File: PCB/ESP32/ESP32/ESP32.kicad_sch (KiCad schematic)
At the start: 31 parts, among them J1 Camera_Receptacle_THT, J1 Conn_01x02_Pin, J1 USB_B_Micro, J2 Conn_01x02_Socket, SW1 RESET, SW2 BOOT, SW3 LRA Switch, U1 DRV2605LTDGSRQ1, U1 ESP32-S2-SOLO-U-N4, U1 MCP73832T-2ACI/OT

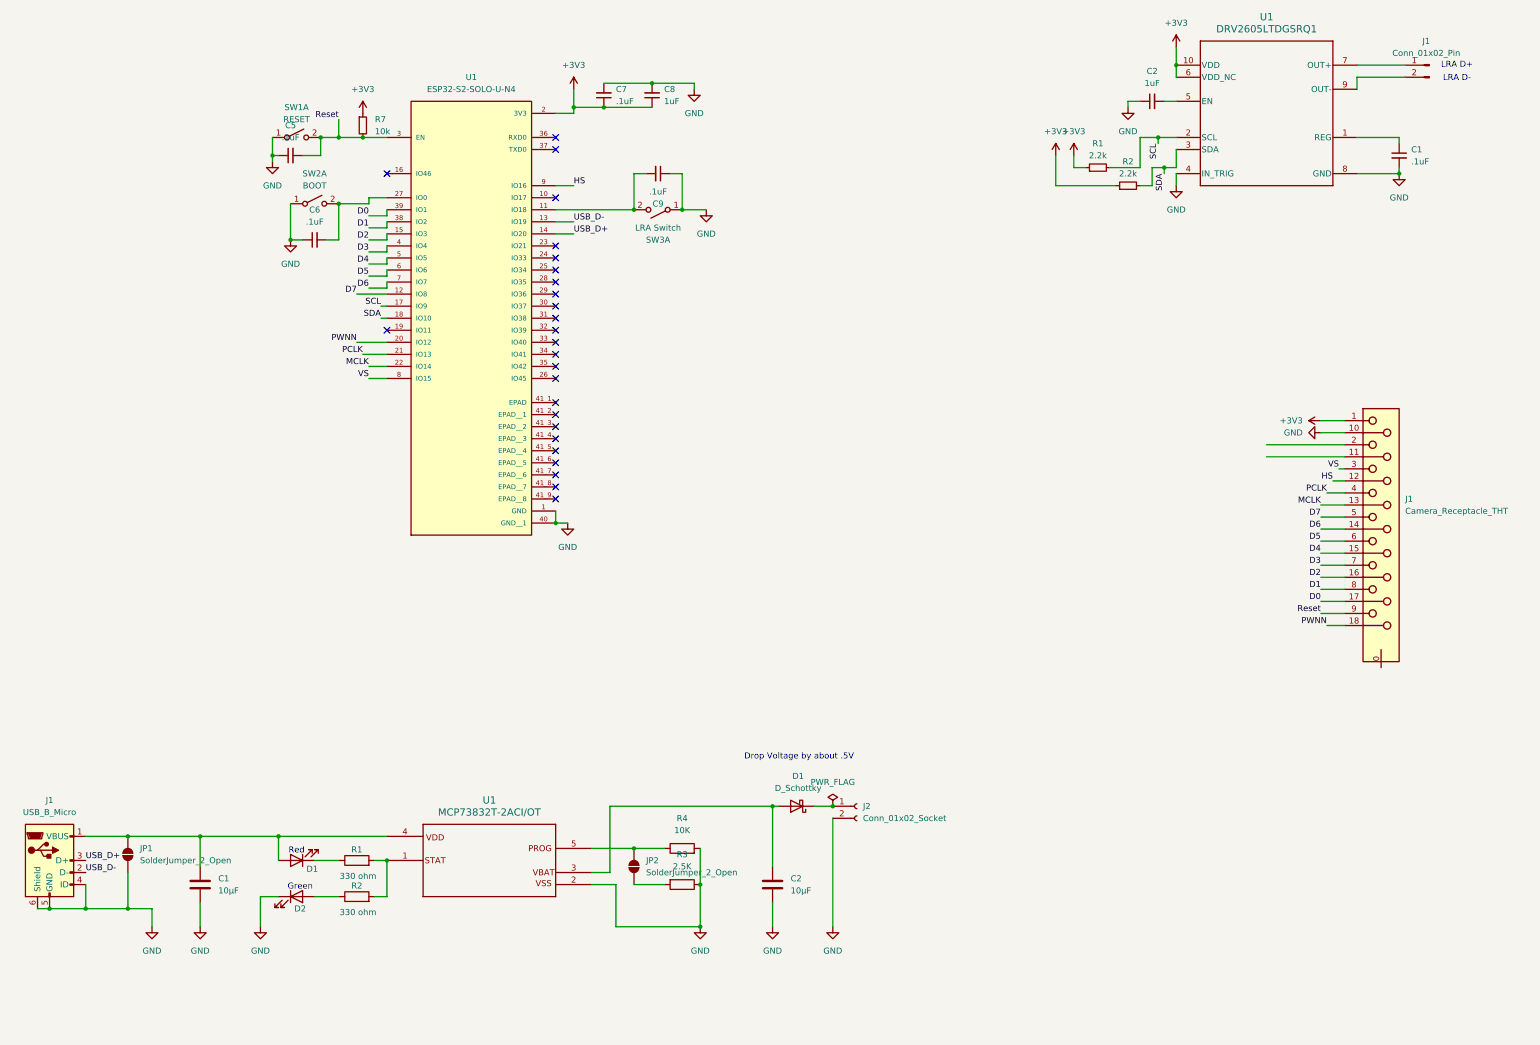
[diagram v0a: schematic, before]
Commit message: Updated camera
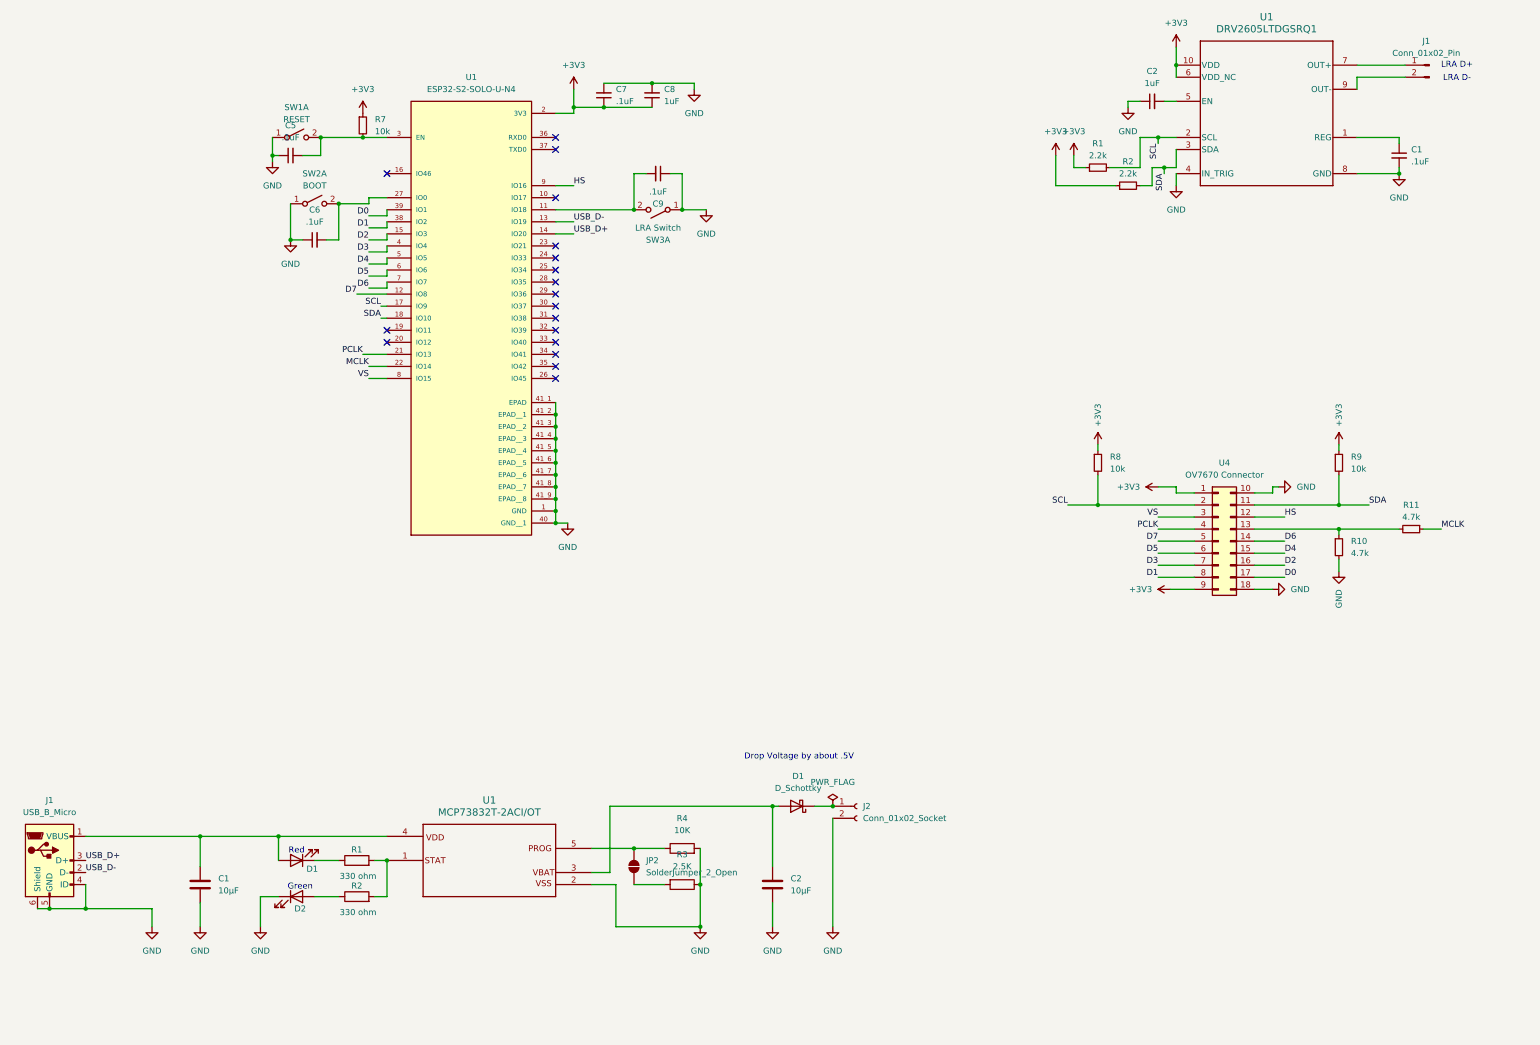
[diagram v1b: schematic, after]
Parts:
- removed J1: Camera_Receptacle_THT, symbol Connector:DA15_Receptacle_MountingHoles
- removed JP1: SolderJumper_2_Open, Jumper:SolderJumper-2_P1.3mm_Bridged2Bar_Pad1.0x1.5mm, symbol Jumper:SolderJumper_2_Open
- added R10, R11: 4.7k, Resistor_SMD:R_0603_1608Metric, symbol Device:R_Small
- added R8, R9: 10k, Resistor_SMD:R_0805_2012Metric, symbol Device:R_Small
- added U4: OV7670 Connector, symbol Connector_Generic:Conn_02x09_Top_Bottom
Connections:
- net +3V3: now also R8.1, R9.1, U4.1 (Pin_1), U4.9 (Pin_9)
- net D0: now also U4.17 (Pin_17)
- net D1: now also U4.8 (Pin_8)
- net D2: now also U4.16 (Pin_16)
- net D3: now also U4.7 (Pin_7)
- net D4: now also U4.15 (Pin_15)
- net D5: now also U4.6 (Pin_6)
- net D6: now also U4.14 (Pin_14)
- net D7: now also U4.5 (Pin_5)
- net GND: now also U1.41_1 (EPAD), U1.41_2 (EPAD__1), U1.41_3 (EPAD__2), U1.41_4 (EPAD__3), U1.41_5 (EPAD__4), U1.41_6 (EPAD__5), U1.41_7 (EPAD__6), U1.41_8 (EPAD__7), U1.41_9 (EPAD__8), R10.2, U4.10 (Pin_10), U4.18 (Pin_18)
- net HS: now also U4.12 (Pin_12)
- net MCLK: now also R11.1
- net PCLK: now also U4.4 (Pin_4)
- net SCL: now also R8.2, U4.2 (Pin_2)
- net SDA: now also R9.2, U4.11 (Pin_11)
- net VS: now also U4.3 (Pin_3)
- net PWNN: no longer names the net of U1.20 (IO12)
- net Reset: no longer names the net of C5.2, R7.2, SW1.2 (B), U1.3 (EN)
- new net: R10.1, R11.2, U4.13 (Pin_13)
- no-connect marks 26 -> 18

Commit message: Charging schematic done
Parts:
- removed C1, C2: 10μF, Capacitor_SMD:C_0603_1608Metric_Pad1.08x0.95mm_HandSolder, symbol Device:C
- removed D1, D2: LED, Diode_SMD:D_0603_1608Metric_Pad1.05x0.95mm_HandSolder, symbol Device:LED
- removed J1: USB_B_Micro, ESP32_sym_footprint:CONN_10118193-0001LF_AMP, symbol Connector:USB_B_Micro
- removed J2: Conn_01x02_Socket, ESP32_sym_footprint:CONN2_B2B-PH-K-S_JST, symbol Connector:Conn_01x02_Socket
- removed R1, R2: 330 ohm, Resistor_SMD:R_0603_1608Metric_Pad0.98x0.95mm_HandSolder, symbol Device:R
- removed R3: 2.5K, Resistor_SMD:R_0603_1608Metric_Pad0.98x0.95mm_HandSolder, symbol Device:R
- added C3, C4: 1uF, symbol Device:C
- added C8: 10μF, Capacitor_SMD:C_0603_1608Metric_Pad1.08x0.95mm_HandSolder, symbol Device:C
- added D4, D5: LED, Diode_SMD:D_0603_1608Metric_Pad1.05x0.95mm_HandSolder, symbol Device:LED
- added J4: Conn_01x02_Socket, ESP32_sym_footprint:CONN2_B2B-PH-K-S_JST, symbol Connector:Conn_01x02_Socket
- added J5: USB_B_Micro, ESP32_sym_footprint:CONN_10118193-0001LF_AMP, symbol Connector:USB_B_Micro
- added Q1: PMOS, symbol Simulation_SPICE:PMOS
- added R12, R13: 330 ohm, Resistor_SMD:R_0603_1608Metric_Pad0.98x0.95mm_HandSolder, symbol Device:R
- added R18: 10K, Resistor_SMD:R_0603_1608Metric_Pad0.98x0.95mm_HandSolder, symbol Device:R
- added R19: 2.5K, Resistor_SMD:R_0603_1608Metric_Pad0.98x0.95mm_HandSolder, symbol Device:R
- added U3: AP2112K-3.3, Package_TO_SOT_SMD:SOT-23-5, symbol Regulator_Linear:AP2112K-3.3
- D1: footprint ESP32_sym_footprint:DO-41_STM -> (none)
- R4: value 10K -> 10k; footprint Resistor_SMD:R_0603_1608Metric_Pad0.98x0.95mm_HandSolder -> (none)
- U1: footprint ESP32_sym_footprint:SOT-23-5_MC_MCH -> SOT-23-5_MC_MCH
- renumbered C5 to C2, C6 to C3, C7 to C4, C8 to C5, C9 to C6, R9 to R14, R10 to R15, R11 to R16, R7 to R3, R8 to R9, U1 to U2, U4 to U3
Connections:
- net GND: now also C3.1, C4.2, C8.2, D5.1 (K), J4.2 (Pin_2), J5.4 (ID), J5.5 (GND), J5.6 (Shield), R18.2, R19.1, U3.2 (GND)
- net USB_D+: now also J5.3 (D+)
- net USB_D-: now also J5.2 (D-)
- net at JP2.1 (A): now also R19.2
- net at JP2.2 (B), U1.5: now also R18.1; no longer R4.1
- net at U1.4: now also D1.2 (A), R4.1, D4.2 (A), J5.1 (VBUS), Q1.2 (G)
- net at D1.1 (K): now also C4.1, U3.5 (VOUT)
- net at U1.3: now also C8.1, J4.1 (Pin_1), Q1.3 (S); no longer D1.2 (A)
- net at U1.1: now also R12.2, R13.2
- new net: C3.2, Q1.1 (D), U3.1 (VIN)
- new net: D4.1 (K), R12.1
- new net: D5.2 (A), R13.1
- new net VCC: U3.3 (EN)
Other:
- note removed: "Drop Voltage by about .5V"

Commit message: ddasd
as
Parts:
- added U1: AP2112K-3.3, Package_TO_SOT_SMD:SOT-23-5, symbol Regulator_Linear:AP2112K-3.3
- C1, C2, C3, C4, C5, C6: footprint Capacitor_SMD:C_0603_1608Metric -> Capacitor_SMD:C_0603_1608Metric_Pad1.08x0.95mm_HandSolder
- C3, C4: footprint (none) -> Capacitor_SMD:C_0603_1608Metric_Pad1.08x0.95mm_HandSolder
- D1: footprint (none) -> zzzzz:SOT-23-5_MC_MCH
- J1, J4: footprint ESP32_sym_footprint:CONN2_B2B-PH-K-S_JST -> zzzzz:CONN2_B2B-PH-K-S_JST
- J5: footprint ESP32_sym_footprint:CONN_10118193-0001LF_AMP -> zzzzz:CONN_10118193-0001LF_AMP
- R1, R14, R2, R3, R9: footprint Resistor_SMD:R_0805_2012Metric -> Resistor_SMD:R_0603_1608Metric_Pad0.98x0.95mm_HandSolder
- R15, R16: footprint Resistor_SMD:R_0603_1608Metric -> Resistor_SMD:R_0603_1608Metric_Pad0.98x0.95mm_HandSolder
- R4: footprint (none) -> Resistor_SMD:R_0603_1608Metric_Pad0.98x0.95mm_HandSolder
- U1: footprint SOT-23-5_MC_MCH -> zzzzz:SOT-23-5_MC_MCH
- U1: footprint ESP32_sym_footprint:DGS0010A_L -> zzzzz:DGS0010A_L
- U3: footprint (none) -> zzzzz:215307-9_TYC
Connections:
- net +3V3: now also C4.1, D1.1 (K), U3.5 (VOUT)
- net GND: now also U1.2 (GND)
- net at D4.2 (A), J5.1 (VBUS), Q1.2 (G)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: now also U1.1 (VIN), U1.3 (EN); no longer D1.2 (A)
- new net: D1.2 (A), U1.5 (VOUT)
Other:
- moved on the sheet: D1

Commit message: das
dasdas
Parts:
- removed R14, R9: 10k, Resistor_SMD:R_0603_1608Metric_Pad0.98x0.95mm_HandSolder, symbol Device:R_Small
- removed R15, R16: 4.7k, Resistor_SMD:R_0603_1608Metric_Pad0.98x0.95mm_HandSolder, symbol Device:R_Small
- removed U1: AP2112K-3.3, Package_TO_SOT_SMD:SOT-23-5, symbol Regulator_Linear:AP2112K-3.3
- removed U3: OV7670 Connector, zzzzz:215307-9_TYC, symbol Connector_Generic:Conn_02x09_Top_Bottom
- added D1: D_Schottky, zzzzz:SOT-23-5_MC_MCH, symbol Device:D_Schottky
- added J1, J2: PPTC091LFBN-RC, CONN9_PPTC091LFBN-RC_SUL, symbol 1x9_header:PPTC091LFBN-RC
- added R1, R5: 10k, Resistor_SMD:R_0603_1608Metric_Pad0.98x0.95mm_HandSolder, symbol Device:R_Small
- added R2, R4: 4.7k, Resistor_SMD:R_0603_1608Metric_Pad0.98x0.95mm_HandSolder, symbol Device:R_Small
- Q1: footprint (none) -> zzzzz:SOT65P210X110-3N
- SW1, SW2, SW3: footprint ESP32_sym_footprint:SW_TL59AF160Q_EWI -> zzzzz:B3U-1000P
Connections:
- net VCC is gone; now on an unnamed net: U3.3 (EN)
- net +3V3: now also J1.1, J1.9, R1.1, R5.1; no longer D1.1 (K)
- net D0: now also J2.8
- net D1: now also J1.8
- net D2: now also J2.7
- net D3: now also J1.7
- net D4: now also J2.6
- net D5: now also J1.6
- net D6: now also J2.5
- net D7: now also J1.5
- net GND: now also J2.1, J2.9, R2.2
- net HS: now also J2.3
- net MCLK: now also R4.1
- net PCLK: now also J1.4
- net SCL: now also J1.2, R5.2
- net SDA: now also J2.2, R1.2
- net VS: now also J1.3
- net at D4.2 (A), J5.1 (VBUS), Q1.2 (G)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: now also D1.2 (A)
- net at C3.2, U3.1 (VIN): now also D1.1 (K), D1.1 (K); no longer Q1.1 (D)
- new net: J2.4, R2.1, R4.2
- new net: D1.2 (A), Q1.1 (D)
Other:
- moved on the sheet: C3, D1

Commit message: New and improved footprint. Started layout
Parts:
- D1, U1: footprint zzzzz:SOT-23-5_MC_MCH -> Footprint:SOT-23-5_MC_MCH
- J1, J4: footprint zzzzz:CONN2_B2B-PH-K-S_JST -> Footprint:CONN2_B2B-PH-K-S_JST
- J1, J2: footprint CONN9_PPTC091LFBN-RC_SUL -> Footprint:CONN9_PPTC091LFBN-RC_SUL
- J5: footprint zzzzz:CONN_10118193-0001LF_AMP -> Footprint:CONN_10118193-0001LF_AMP
- Q1: footprint zzzzz:SOT65P210X110-3N -> Footprint:SOT65P210X110-3N
- SW1, SW2, SW3: footprint zzzzz:B3U-1000P -> Footprint:B3U-1000P
- U1: footprint zzzzz:DGS0010A_L -> Footprint:DGS0010A_L
- U2: footprint ESP32_sym_footprint:XCVR_ESP32-S2-SOLO-U-N4 -> Footprint:XCVR_ESP32-S2-SOLO-U-N4
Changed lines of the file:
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@@
 	(label "D7"
 		(at 102.87 78.74 180)
+		(fields_autoplaced yes)
 		(effects
 			(font
@@
 	(label "USB_D+"
 		(at 44.45 200.66 0)
+		(fields_autoplaced yes)
 		(effects
 			(font
@@
 	(label "SDA"
 		(at 273.05 53.34 270)
+		(fields_autoplaced yes)
 		(effects
 			(font
@@
 	(label "SDA"
 		(at 316.23 119.38 0)
+		(fields_autoplaced yes)
 		(effects
 			(font
@@
 	(label "D6"
 		(at 298.45 127 0)
+		(fields_autoplaced yes)
 		(effects
 			(font
@@
 	(label "D3"
 		(at 105.41 69.85 180)
+		(fields_autoplaced yes)
 		(effects
 			(font
@@
 	(label "D0"
 		(at 298.45 134.62 0)
+		(fields_autoplaced yes)
 		(effects
 			(font
@@
 	(label "VS"
 		(at 105.41 96.52 180)
+		(fields_autoplaced yes)
 		(effects
 			(font
@@
 	(label "USB_D-"
 		(at 44.45 203.2 0)
+		(fields_autoplaced yes)
 		(effects
 			(font
@@
 	(label "D6"
 		(at 105.41 77.47 180)
+		(fields_autoplaced yes)
 		(effects
 			(font
@@
 	(label "D7"
 		(at 259.08 127 180)
+		(fields_autoplaced yes)
 		(effects
 			(font
@@
 	(label "D5"
 		(at 259.08 129.54 180)
+		(fields_autoplaced yes)
 		(effects
 			(font
@@
 	(label "VS"
 		(at 259.08 121.92 180)
+		(fields_autoplaced yes)
 		(effects
 			(font
@@
 	(label "MCLK"
 		(at 331.47 124.46 0)
+		(fields_autoplaced yes)
 		(effects
 			(font
@@
 	(label "SCL"
 		(at 107.95 81.28 180)
+		(fields_autoplaced yes)
 		(effects
 			(font
@@
 	(label "D4"
 		(at 105.41 72.39 180)
+		(fields_autoplaced yes)
 		(effects
 			(font
@@
 	(label "SCL"
 		(at 240.03 119.38 180)
+		(fields_autoplaced yes)
 		(effects
 			(font
@@
 	(label "MCLK"
 		(at 105.41 93.98 180)
+		(fields_autoplaced yes)
 		(effects
 			(font
@@
 	(label "D0"
 		(at 105.41 62.23 180)
+		(fields_autoplaced yes)
 		(effects
 			(font
@@
 	(label "D2"
 		(at 298.45 132.08 0)
+		(fields_autoplaced yes)
 		(effects
 			(font
@@
 	(label "USB_D-"
 		(at 148.59 63.5 0)
+		(fields_autoplaced yes)
 		(effects
 			(font
@@
 	(label "USB_D+"
 		(at 148.59 66.04 0)
+		(fields_autoplaced yes)
 		(effects
 			(font
@@
 	(label "PCLK"
 		(at 259.08 124.46 180)
+		(fields_autoplaced yes)
 		(effects
 			(font
@@
 	(label "SDA"
 		(at 107.95 83.82 180)
+		(fields_autoplaced yes)
 		(effects
 			(font
@@
 	(label "PCLK"
 		(at 104.14 91.44 180)
+		(fields_autoplaced yes)
 		(effects
 			(font
@@
 	(label "D4"
 		(at 298.45 129.54 0)
+		(fields_autoplaced yes)
 		(effects
 			(font
@@
 	(label "D1"
 		(at 105.41 64.77 180)
+		(fields_autoplaced yes)
 		(effects
 			(font
@@
 	(label "D1"
 		(at 259.08 134.62 180)
+		(fields_autoplaced yes)
 		(effects
 			(font
@@
 	(label "D2"
 		(at 105.41 67.31 180)
+		(fields_autoplaced yes)
 		(effects
 			(font
@@
 	(label "D3"
 		(at 259.08 132.08 180)
+		(fields_autoplaced yes)
 		(effects
 			(font
@@
 	(label "HS"
 		(at 298.45 121.92 0)
+		(fields_autoplaced yes)
 		(effects
 			(font
@@
 	(label "D5"
 		(at 105.41 74.93 180)
+		(fields_autoplaced yes)
 		(effects
 			(font
@@
 	(label "HS"
 		(at 148.59 55.88 0)
+		(fields_autoplaced yes)
 		(effects
 			(font
@@
 	(label "SCL"
 		(at 271.78 46.99 270)
+		(fields_autoplaced yes)
 		(effects
 			(font
@@
 			)
 		)
-		(property "Footprint" "zzzzz:CONN2_B2B-PH-K-S_JST"
+		(property "Footprint" "Footprint:CONN2_B2B-PH-K-S_JST"
 			(at 328.93 30.48 0)
 			(effects
@@
 			)
 		)
-		(property "Footprint" "ESP32_sym_footprint:XCVR_ESP32-S2-SOLO-U-N4"
+		(property "Footprint" "Footprint:XCVR_ESP32-S2-SOLO-U-N4"
 			(at 127 71.12 0)
 			(effects
@@
 			)
 		)
-		(property "Footprint" "zzzzz:B3U-1000P"
+		(property "Footprint" "Footprint:B3U-1000P"
 			(at 166.37 60.96 0)
 			(effects
@@
 			)
 		)
-		(property "Footprint" "zzzzz:CONN2_B2B-PH-K-S_JST"
+		(property "Footprint" "Footprint:CONN2_B2B-PH-K-S_JST"
 			(at 156.21 217.17 0)
 			(effects
@@
 			)
 		)
-		(property "Footprint" "zzzzz:SOT-23-5_MC_MCH"
+		(property "Footprint" "Footprint:SOT-23-5_MC_MCH"
 			(at 93.472 184.912 0)
 			(effects
@@
 			)
 		)
-		(property "Footprint" "CONN9_PPTC091LFBN-RC_SUL"
+		(property "Footprint" "Footprint:CONN9_PPTC091LFBN-RC_SUL"
 			(at 271.78 115.57 0)
 			(effects
@@
 			)
 		)
-		(property "Footprint" "zzzzz:DGS0010A_L"
+		(property "Footprint" "Footprint:DGS0010A_L"
 			(at 293.37 40.64 0)
 			(effects
@@
 			)
 		)
-		(property "Footprint" "CONN9_PPTC091LFBN-RC_SUL"
+		(property "Footprint" "Footprint:CONN9_PPTC091LFBN-RC_SUL"
 			(at 287.02 115.57 0)
 			(effects
@@
 			)
 		)
-		(property "Footprint" "zzzzz:SOT-23-5_MC_MCH"
+		(property "Footprint" "Footprint:SOT-23-5_MC_MCH"
 			(at 151.13 184.15 0)
 			(effects
@@
 			)
 		)
-		(property "Footprint" "zzzzz:B3U-1000P"
+		(property "Footprint" "Footprint:B3U-1000P"
 			(at 90.17 45.72 0)
 			(effects
@@
 			)
 		)
-		(property "Footprint" "zzzzz:SOT-23-5_MC_MCH"
+		(property "Footprint" "Footprint:SOT-23-5_MC_MCH"
 			(at 151.13 172.72 0)
 			(effects
@@
 			)
 		)
-		(property "Footprint" "zzzzz:CONN_10118193-0001LF_AMP"
+		(property "Footprint" "Footprint:CONN_10118193-0001LF_AMP"
 			(at 40.64 201.93 0)
 			(effects
@@
 			)
 		)
-		(property "Footprint" "zzzzz:B3U-1000P"
+		(property "Footprint" "Footprint:B3U-1000P"
 			(at 93.98 59.69 0)
 			(effects
@@
 			)
 		)
-		(property "Footprint" "zzzzz:SOT65P210X110-3N"
+		(property "Footprint" "Footprint:SOT65P210X110-3N"
 			(at 153.67 190.5 0)
 			(effects
